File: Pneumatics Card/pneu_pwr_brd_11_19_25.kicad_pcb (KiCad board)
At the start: 4 copper layers, 65 x 65 mm, 95 parts, among them J1 2X1, J10 Conn_01x02, J11 Conn_01x02, J12 2X1, J13 2X1, J2 2X1, J3 2X1, J4 2X1, J5 2X1, J6 2X1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

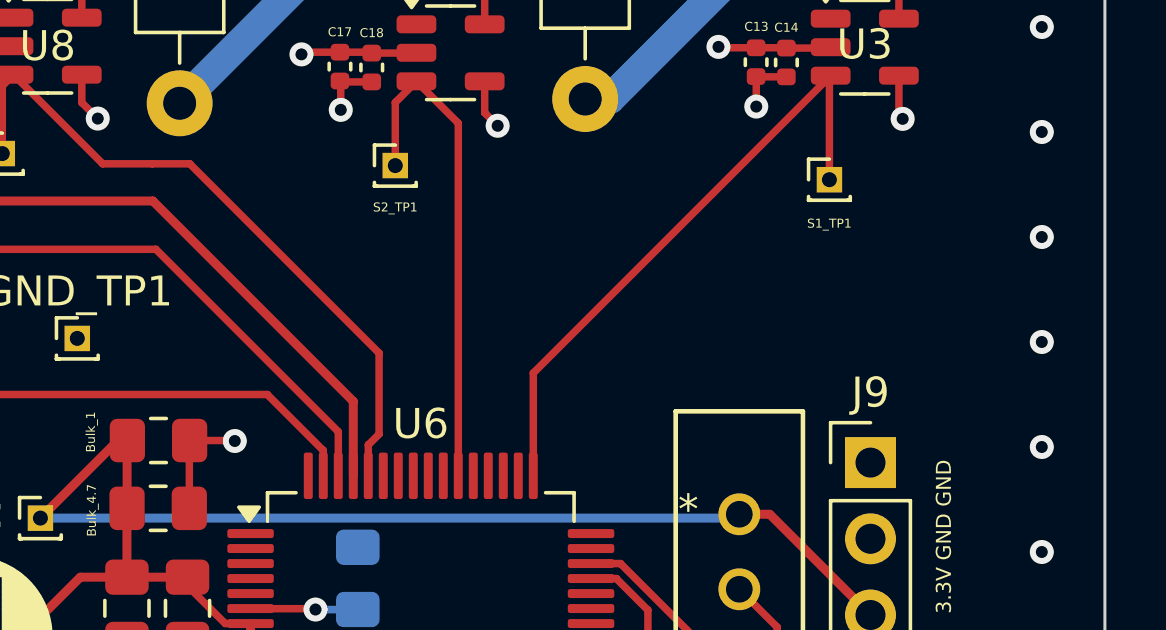
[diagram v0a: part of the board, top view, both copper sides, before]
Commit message: Added R@M Silkscreen
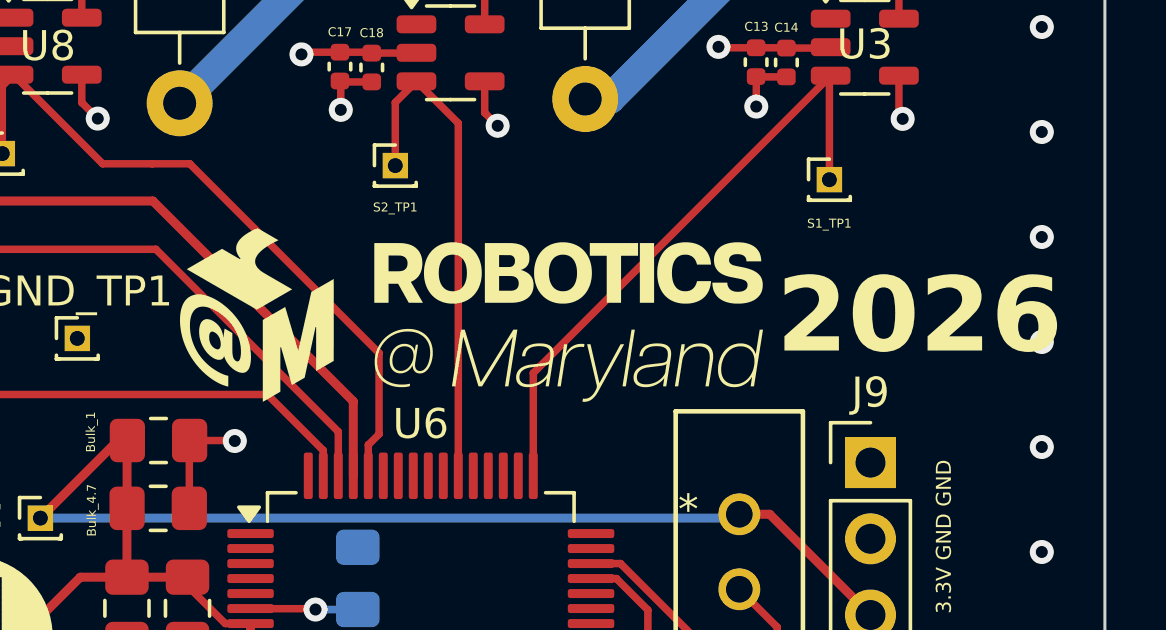
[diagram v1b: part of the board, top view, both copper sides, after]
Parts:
- added G***: LOGO, LOGO, F.Cu at (121.8, 51.3)
- added G***: LOGO, LOGO, B.Cu at (107.0, 53.0)
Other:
- board text added: "2026"

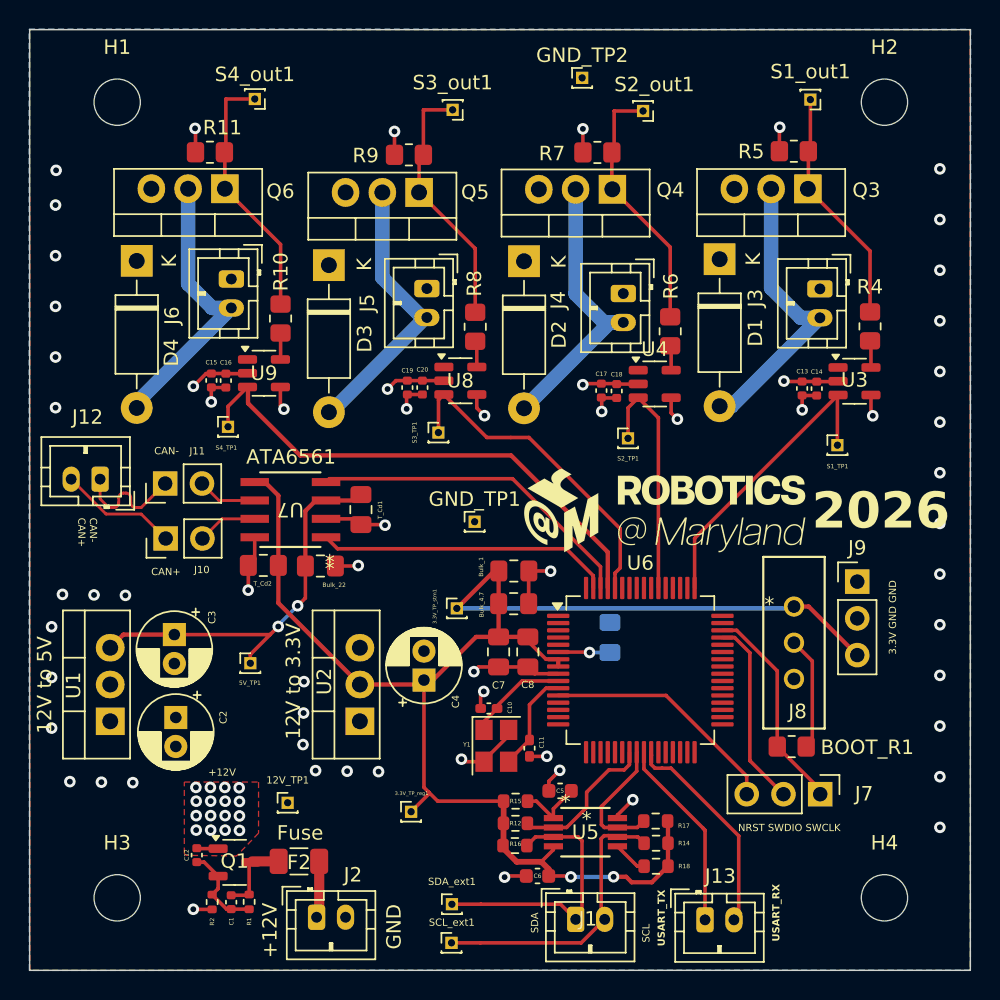
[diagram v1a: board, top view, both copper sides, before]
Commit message: Created Production Files, Sized Up Silkscreen
Pneumatics Gerber 2026 is the zip file used in the order. I will clean up the other ones later.
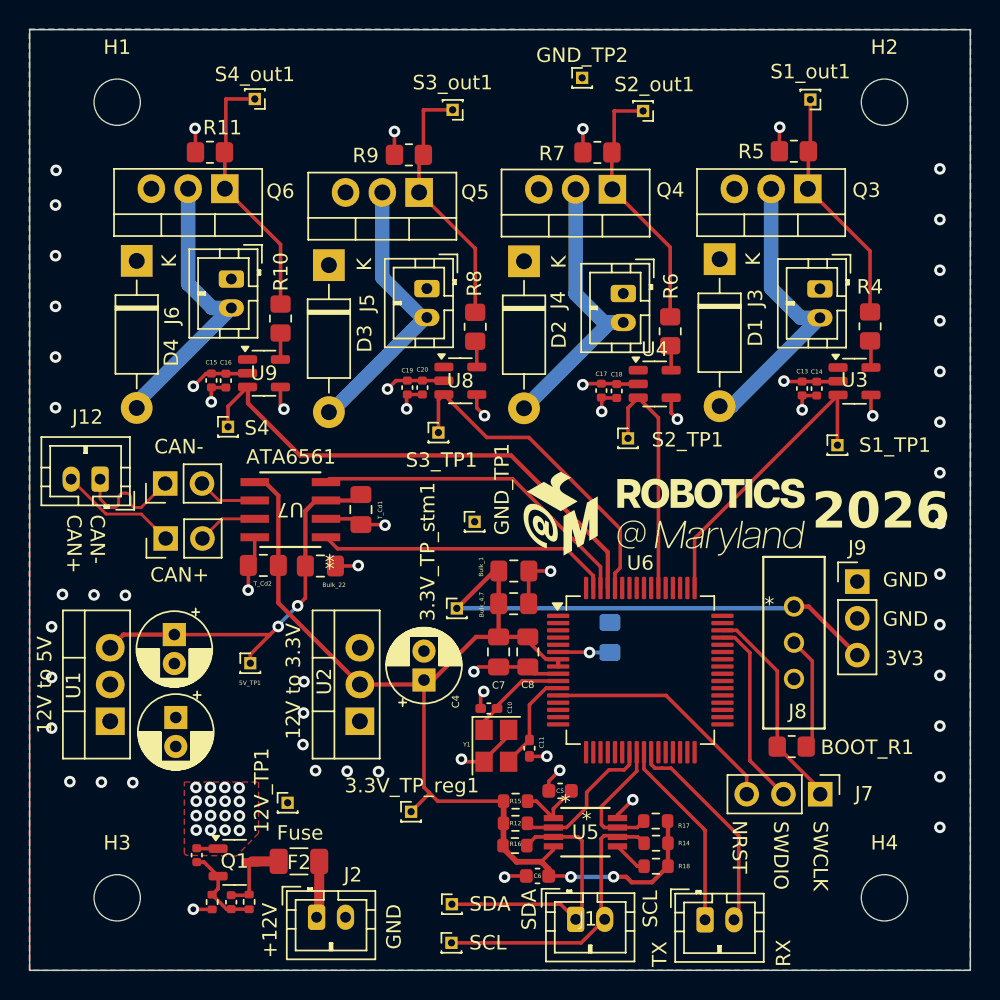
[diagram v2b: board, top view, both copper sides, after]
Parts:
- moved G*** 0.23 mm to (121.8, 51.6)
- renumbered SCL_ext1 to SCL, SDA_ext1 to SDA
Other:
- board text added: "3V3"
- board text added: "NRST"
- board text added: "RX"
- board text added: "S4"
- board text added: "SWCLK"
- board text added: "SWDIO"
- board text added: "TX"
- board text removed: "3.3V GND GND"
- board text removed: "NRST SWDIO SWCLK"
- board text removed: "USART_RX"
- board text removed: "USART_TX"
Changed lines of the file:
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@@
 			(plot_on_all_layers_selection 0x00000000_00000000_00000000_00000000)
 			(disableapertmacros no)
-			(usegerberextensions no)
+			(usegerberextensions yes)
 			(usegerberattributes yes)
 			(usegerberadvancedattributes yes)
-			(creategerberjobfile yes)
+			(creategerberjobfile no)
 			(dashed_line_dash_ratio 12.000000)
 			(dashed_line_gap_ratio 3.000000)
@@
 			(drillshape 0)
 			(scaleselection 1)
-			(outputdirectory "./")
+			(outputdirectory "Pneumatics Gerber 2026/")
 		)
 	)
@@
 			(at 2.24 2.21 180)
 			(layer "F.SilkS")
+			(hide yes)
 			(effects
 				(font
@@
 			(at -1.33 0.0125 90)
 			(layer "F.SilkS")
+			(hide yes)
 			(effects
 				(font
@@
 		(tags "Through hole pin header THT 1x01 1.00mm single row")
 		(property "Reference" "S1_TP1"
-			(at 0 1.46 0)
+			(at 3.97 0 0)
 			(layer "F.SilkS")
 			(effects
 				(font
-					(size 0.3 0.3)
-					(thickness 0.0375)
+					(size 1 1)
+					(thickness 0.125)
 				)
 			)
@@
 		(descr "Through hole straight pin header, 1x01, 1.00mm pitch, single row")
 		(tags "Through hole pin header THT 1x01 1.00mm single row")
-		(property "Reference" "SCL_ext1"
-			(at 0.02 -1.41 0)
+		(property "Reference" "SCL"
+			(at 2.69 -0.01 0)
 			(layer "F.SilkS")
+			(hide yes)
 			(effects
 				(font
-					(size 0.5 0.5)
-					(thickness 0.0625)
+					(size 1 1)
+					(thickness 0.125)
 				)
 			)
@@
 		(tags "Through hole pin header THT 1x01 1.00mm single row")
 		(property "Reference" "S2_TP1"
-			(at 0 1.39 0)
+			(at 4.11 0.1 0)
 			(layer "F.SilkS")
 			(effects
 				(font
-					(size 0.3 0.3)
-					(thickness 0.0375)
+					(size 1 1)
+					(thickness 0.125)
 				)
 			)
@@
 		(descr "Through hole straight pin header, 1x01, 1.00mm pitch, single row")
 		(tags "Through hole pin header THT 1x01 1.00mm single row")
-		(property "Reference" "SDA_ext1"
-			(at 0 -1.56 0)
+		(property "Reference" "SDA"
+			(at 2.59 -0.02 0)
 			(layer "F.SilkS")
+			(hide yes)
 			(effects
 				(font
-					(size 0.5 0.5)
-					(thickness 0.0625)
+					(size 1 1)
+					(thickness 0.125)
 				)
 			)
@@
 			(at 1.06 -3.02 0)
 			(layer "F.SilkS")
+			(hide yes)
 			(effects
 				(font
@@
 		(tags "Through hole pin header THT 1x01 1.00mm single row")
 		(property "Reference" "S4_TP1"
-			(at -0.12 1.45 0)
+			(at 3.78 0.24 0)
 			(layer "F.SilkS")
+			(hide yes)
 			(effects
 				(font
-					(size 0.3 0.3)
-					(thickness 0.0375)
+					(size 1 1)
+					(thickness 0.125)
 				)
 			)
@@
 		(tags "Through hole pin header THT 1x01 1.00mm single row")
 		(property "Reference" "S3_TP1"
-			(at -1.65 0 90)
+			(at 0.21 1.9 180)
 			(layer "F.SilkS")
 			(effects
 				(font
-					(size 0.3 0.3)
-					(thickness 0.0375)
+					(size 1 1)
+					(thickness 0.125)
 				)
 			)
@@
 			(at -0.01 -3.28 90)
 			(layer "F.SilkS")
+			(hide yes)
 			(effects
 				(font
@@
 			(at -2.16 2.5 180)
 			(layer "F.SilkS")
+			(hide yes)
 			(effects
 				(font
@@
 		(tags "Through hole pin header THT 1x01 1.00mm single row")
 		(property "Reference" "GND_TP1"
-			(at 0 -1.56 0)
+			(at 1.89 -2.25 90)
 			(layer "F.SilkS")
 			(effects
 				(font
 					(size 1 1)
-					(thickness 0.15)
+					(thickness 0.125)
 				)
 			)
@@
 		(tags "Through hole pin header THT 1x01 1.00mm single row")
 		(property "Reference" "3.3V_TP_reg1"
-			(at 0.03 -1.27 0)
+			(at 0.06 -1.8 0)
 			(layer "F.SilkS")
 			(effects
 				(font
-					(size 0.25 0.25)
-					(thickness 0.03125)
+					(size 1 1)
+					(thickness 0.125)
 				)
 			)
@@
 			(at -1.36 0 90)
 			(layer "F.SilkS")
+			(hide yes)
 			(effects
 				(font
@@
 			(at -1.36 0 90)
 			(layer "F.SilkS")
+			(hide yes)
 			(effects
 				(font
@@
 			(at -1.19 -2.6 90)
 			(layer "F.SilkS")
+			(hide yes)
 			(effects
 				(font
@@
 			(at 0 -0.7 90)
 			(layer "F.SilkS")
+			(hide yes)
 			(effects
 				(font
@@
 	(footprint "LOGO"
 		(layer "F.Cu")
-		(at 121.790913 51.321175)
+		(at 121.750913 51.551175)
 		(property "Reference" "G***"
 			(at 0 0 0)
@@
 		(tags "Through hole pin header THT 1x01 1.00mm single row")
 		(property "Reference" "3.3V_TP_stm1"
-			(at -1.53 -0.13 90)
+			(at -2.01 -3.92 90)
 			(layer "F.SilkS")
 			(effects
 				(font
-					(size 0.25 0.25)
-					(thickness 0.03125)
+					(size 1 1)
+					(thickness 0.125)
 				)
 			)
@@
 		(tags "Through hole pin header THT 1x01 1.00mm single row")
 		(property "Reference" "12V_TP1"
-			(at 0 -1.56 0)
+			(at -1.79 -0.85 270)
 			(layer "F.SilkS")
 			(effects
 				(font
-					(size 0.5 0.5)
-					(thickness 0.0625)
+					(size 1 1)
+					(thickness 0.125)
 				)
 			)
@@
 		(layer "Edge.Cuts")
 	)
-	(gr_text "USART_TX"
-		(at 122.04 81.39 90)
+	(gr_text "SWCLK"
+		(at 132.14 72.73 270)
 		(layer "F.SilkS")
 		(effects
 			(font
-				(size 0.5 0.5)
-				(thickness 0.1)
-				(bold yes)
+				(size 1 1)
+				(thickness 0.125)
+			)
+			(justify left bottom)
+		)
+	)
+	(gr_text "GND"
+		(at 137.04 59.36 0)
+		(layer "F.SilkS")
+		(effects
+			(font
+				(size 1 1)
+				(thickness 0.125)
+			)
+			(justify left bottom)
+		)
+	)
+	(gr_text "RX"
+		(at 130.77 82.81 90)
+		(layer "F.SilkS")
+		(effects
+			(font
+				(size 1 1)
+				(thickness 0.125)
+			)
+			(justify left bottom)
+		)
+	)
+	(gr_text "S4"
+		(at 92.93 46.16 0)
+		(layer "F.SilkS")
+		(effects
+			(font
+				(size 1 1)
+				(thickness 0.125)
 			)
 			(justify left bottom)
@@
 		)
 	)
-	(gr_text "3.3V GND GND"
-		(at 138.02 61.23 90)
+	(gr_text "SWDIO"
+		(at 129.41 72.73 270)
 		(layer "F.SilkS")
 		(effects
 			(font
-				(size 0.5 0.5)
-				(thickness 0.0625)
+				(size 1 1)
+				(thickness 0.125)
 			)
 			(justify left bottom)
@@
 	)
 	(gr_text "SDA"
-		(at 113.29 80.48 90)
+		(at 113.19 80.28 90)
 		(layer "F.SilkS")
 		(effects
 			(font
-				(size 0.5 0.5)
-				(thickness 0.0625)
+				(size 1 1)
+				(thickness 0.125)
 			)
 			(justify left bottom)
@@
 	)
 	(gr_text "CAN+"
-		(at 86.49 55.8 0)
+		(at 86.42 56.31 0)
 		(layer "F.SilkS")
 		(effects
 			(font
-				(size 0.5 0.5)
-				(thickness 0.0625)
+				(size 1 1)
+				(thickness 0.125)
 			)
 			(justify left bottom)
@@
 		)
 	)
+	(gr_text "TX"
+		(at 122.21 82.82 90)
+		(layer "F.SilkS")
+		(effects
+			(font
+				(size 1 1)
+				(thickness 0.125)
+			)
+			(justify left bottom)
+		)
+	)
 	(gr_text "ATA6561"
 		(at 93.05 48.16 0)
@@
 		)
 	)
-	(gr_text "+12V"
-		(at 90.43 69.66 0)
+	(gr_text "SCL"
+		(at 121.57 80.11 90)
 		(layer "F.SilkS")
 		(effects
 			(font
-				(size 0.5 0.5)
+				(size 1 1)
 				(thickness 0.125)
 			)
@@
 		(effects
 			(font
-				(size 0.5 0.5)
-				(thickness 0.0625)
+				(size 1 1)
+				(thickness 0.125)
 			)
 			(justify left bottom)
 		)
 	)
-	(gr_text "NRST SWDIO SWCLK\n"
-		(at 127.04 73.49 0)
+	(gr_text "SCL"
+		(at 108.46 81.73 0)
 		(layer "F.SilkS")
 		(effects
 			(font
-				(size 0.5 0.5)
+				(size 1 1)
 				(thickness 0.125)
 			)
@@
 		)
 	)
-	(gr_text "USART_RX"
-		(at 129.96 81.06 90)
+	(gr_text "3V3"
+		(at 137.2 62.08 0)
 		(layer "F.SilkS")
 		(effects
 			(font
-				(size 0.5 0.5)
+				(size 1 1)
 				(thickness 0.125)
-				(bold yes)
 			)
 			(justify left bottom)
 		)
 	)
-	(gr_text "SCL"
-		(at 120.98 81.13 90)
+	(gr_text "SDA"
+		(at 108.47 79.05 0)
+		(layer "F.SilkS")
+		(effects
+			(font
+				(size 1 1)
+				(thickness 0.125)
+			)
+			(justify left bottom)
+		)
+	)
+	(gr_text "NRST"
+		(at 126.55 72.68 270)
+		(layer "F.SilkS")
+		(effects
+			(font
+				(size 1 1)
+				(thickness 0.125)
+			)
+			(justify left bottom)
+		)
+	)
+	(gr_text "GND"
+		(at 137.04 56.65 0)
 		(layer "F.SilkS")
 		(effects
 			(font
-				(size 0.5 0.5)
+				(size 1 1)
 				(thickness 0.125)
 			)
@@
 	)
 	(gr_text "CAN-\nCAN+"
-		(at 81.39 51.77 270)
+		(at 80.57 51.55 270)
 		(layer "F.SilkS")
 		(effects
 			(font
-				(size 0.5 0.5)
-				(thickness 0.0625)
+				(size 1 1)
+				(thickness 0.125)
 			)
 			(justify left bottom)
